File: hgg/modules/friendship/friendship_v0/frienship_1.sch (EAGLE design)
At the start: 35 parts, among them IC5 741G66DBV, IC6 741G66DBV, IC7 741G66DBV, IC8 741G66DBV

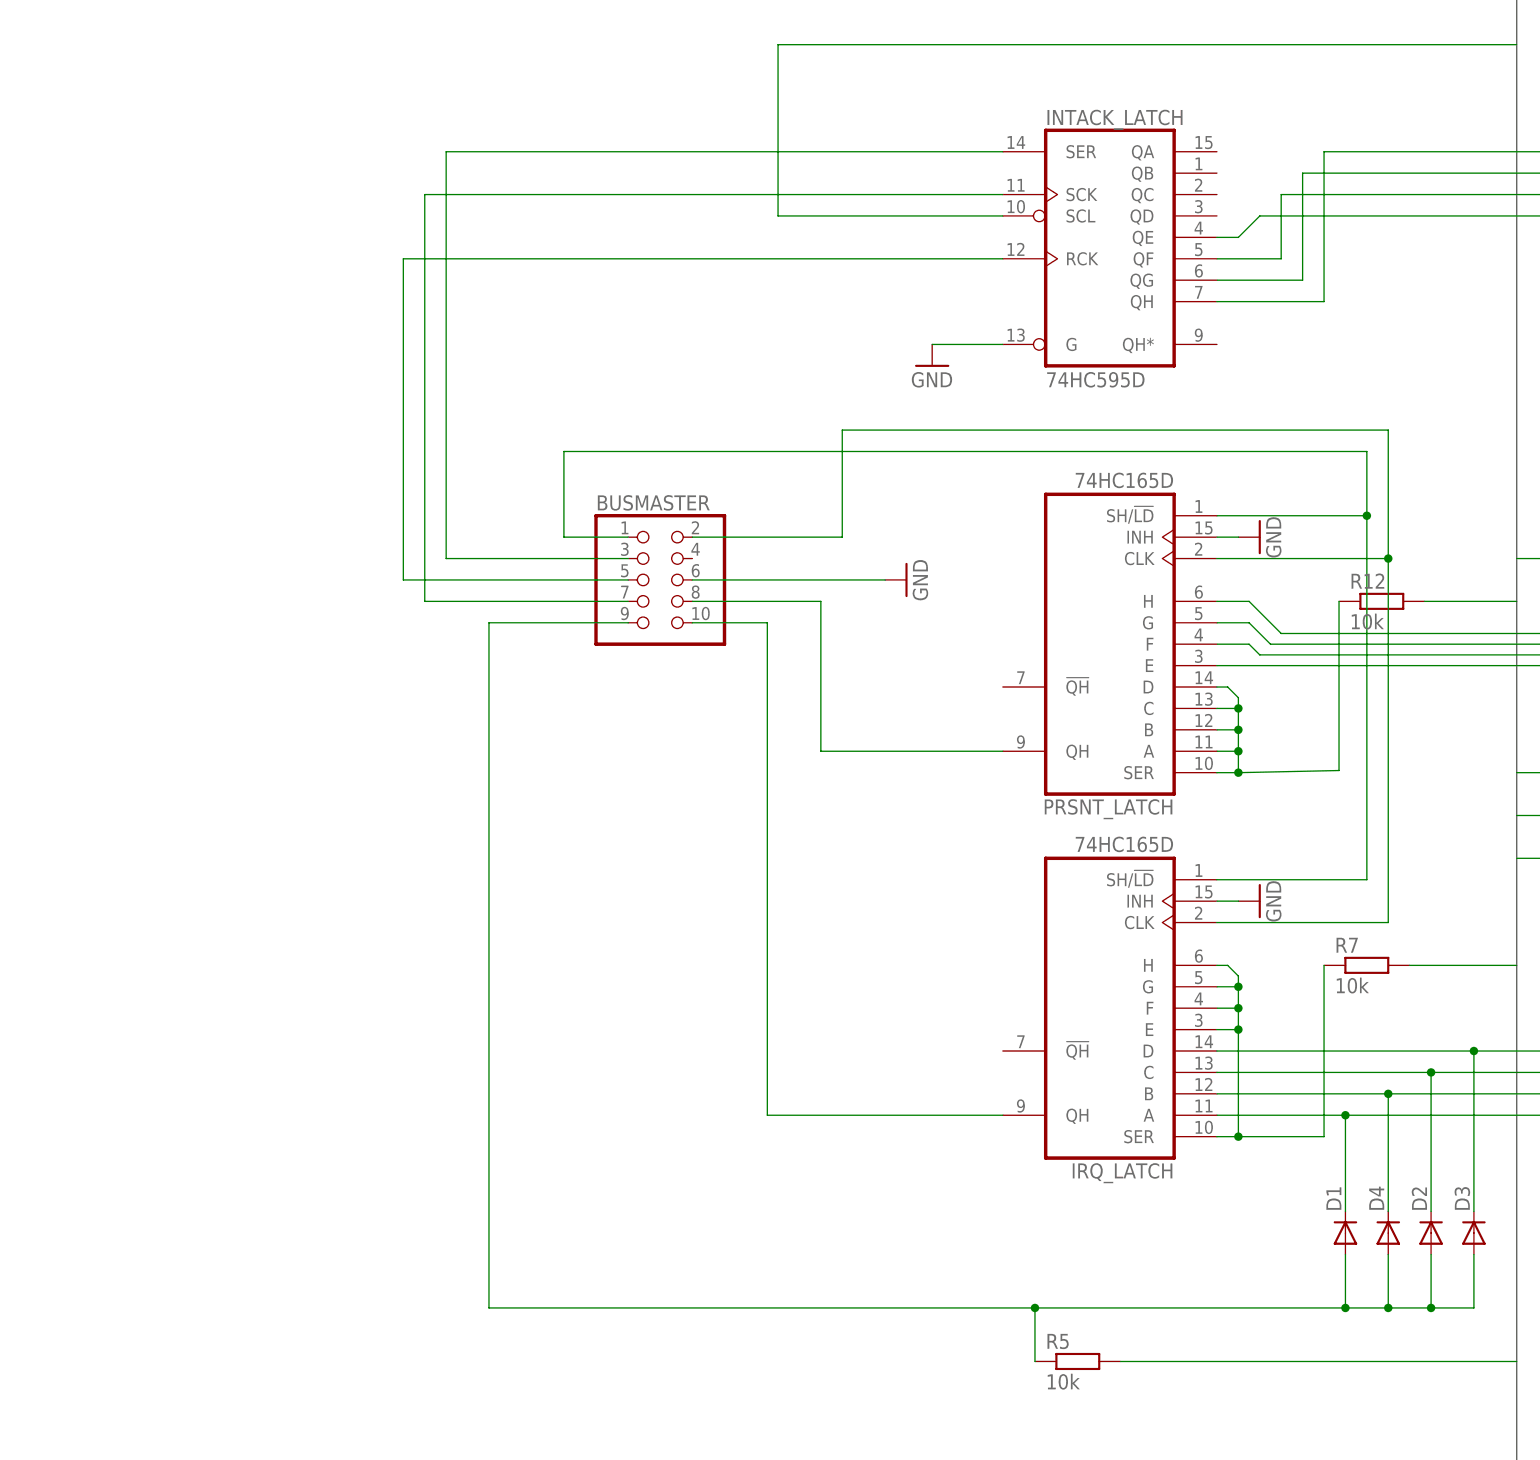
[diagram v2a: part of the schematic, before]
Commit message: using new busmaster plug, more ground vias
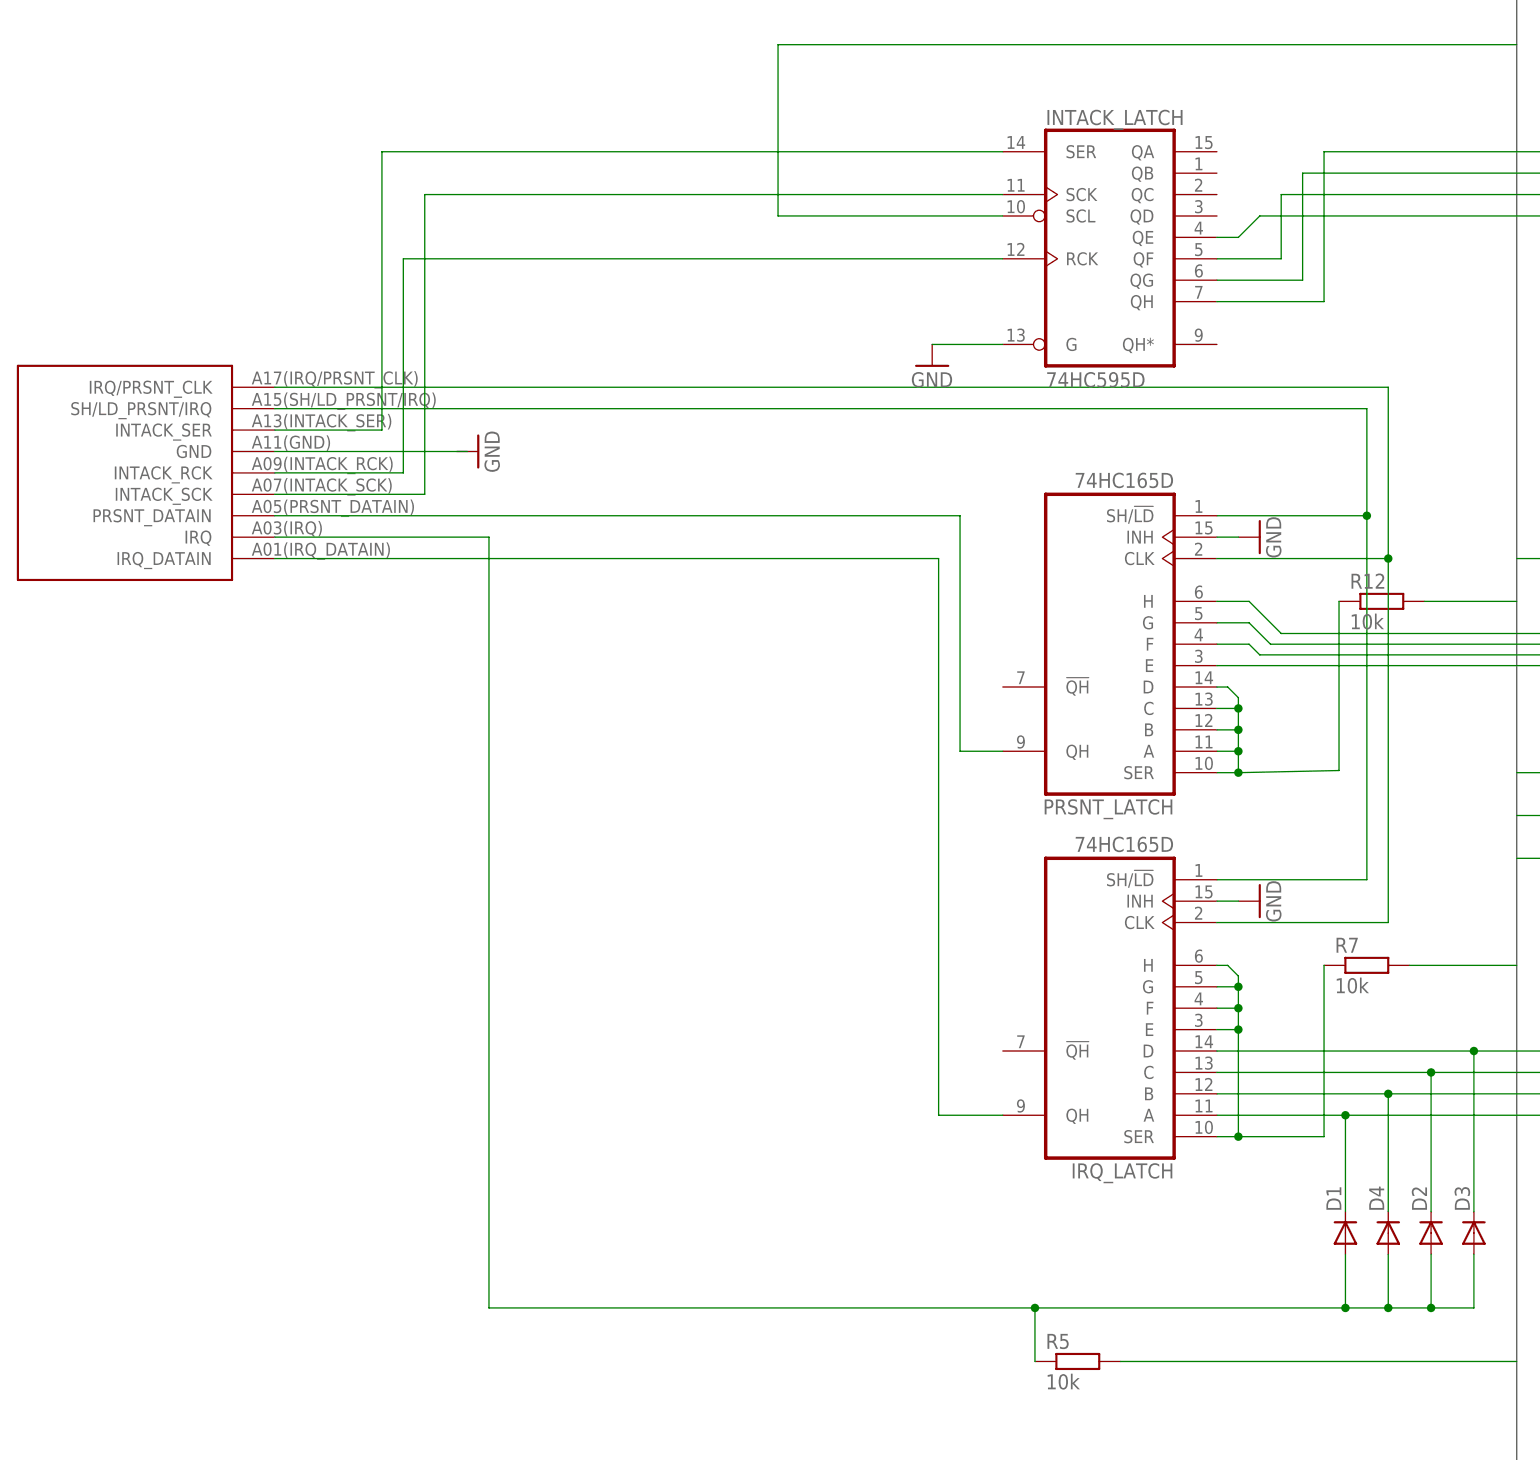
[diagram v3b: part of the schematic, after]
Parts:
- removed BUSMASTER: (no value), pinhead:PINHD-2X5
- added U$1: BUSMASTER_PLUG, hgg:BUSMASTER_PLUG
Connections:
- new net N$12: U$1.GND
- net GND: no longer BUSMASTER.6
- net N$1: now also U$1.INTACK_SER; no longer BUSMASTER.3
- net N$11: now also U$1.IRQ; no longer BUSMASTER.9
- net N$13: now also U$1.PRSNT_DATAIN; no longer BUSMASTER.8
- net N$17: now also U$1.IRQ_DATAIN; no longer BUSMASTER.10
- net N$3: now also U$1.SH/LD_PRSNT/IRQ; no longer BUSMASTER.1
- net N$4: now also U$1.INTACK_SCK; no longer BUSMASTER.7
- net N$9: now also U$1.INTACK_RCK; no longer BUSMASTER.5
- net SHIFT: now also U$1.IRQ/PRSNT_CLK; no longer BUSMASTER.2
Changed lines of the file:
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@@
 <setting verticaltext="up"/>
 </settings>
-<grid distance="0.05" unitdist="inch" unit="inch" style="lines" multiple="1" display="no" altdistance="0.01" altunitdist="inch" altunit="inch"/>
+<grid distance="0.1" unitdist="inch" unit="inch" style="lines" multiple="1" display="no" altdistance="0.01" altunitdist="inch" altunit="inch"/>
 <layers>
 <layer number="1" name="Top" color="4" fill="1" visible="no" active="no"/>
@@
 <part name="IRQ_LATCH" library="74xx-eu" deviceset="74*165" device="D" technology="HC"/>
 <part name="PRSNT_LATCH" library="74xx-eu" deviceset="74*165" device="D" technology="HC"/>
-<part name="BUSMASTER" library="pinhead" deviceset="PINHD-2X5" device=""/>
 <part name="R7" library="rcl" deviceset="R-EU_" device="R0603" value="10k"/>
 <part name="R12" library="rcl" deviceset="R-EU_" device="R0603" value="10k"/>
@@
 <part name="R16" library="rcl" deviceset="R-EU_" device="R0603" value="10k"/>
 <part name="R17" library="rcl" deviceset="R-EU_" device="R0603" value="10k"/>
+<part name="U$1" library="hgg" deviceset="BUSMASTER_PLUG" device=""/>
 </parts>
 <sheets>
@@
 <instance part="IRQ_LATCH" gate="A" x="-157.48" y="-86.36" rot="R180"/>
 <instance part="PRSNT_LATCH" gate="A" x="-157.48" y="-43.18" rot="R180"/>
-<instance part="BUSMASTER" gate="A" x="-212.09" y="-35.56"/>
 <instance part="R7" gate="G$1" x="-127" y="-81.28"/>
 <instance part="R12" gate="G$1" x="-125.222" y="-38.1"/>
@@
 <instance part="D3" gate="G$1" x="-114.3" y="-113.03" rot="R90"/>
 <instance part="D4" gate="G$1" x="-124.46" y="-113.03" rot="R90"/>
-<instance part="GND18" gate="1" x="-181.61" y="-35.56" rot="R90"/>
+<instance part="GND18" gate="1" x="-232.41" y="-20.32" rot="R90"/>
 <instance part="R5" gate="G$1" x="-161.29" y="-128.27"/>
 <instance part="SJ1" gate="1" x="-63.5" y="-302.26"/>
@@
 <instance part="R16" gate="G$1" x="-228.6" y="182.88" rot="R90"/>
 <instance part="R17" gate="G$1" x="-220.98" y="182.88" rot="R90"/>
+<instance part="U$1" gate="G$1" x="-261.62" y="-12.7" rot="R180"/>
 </instances>
 <busses>
@@
 <wire x1="15.24" y1="-185.42" x2="76.2" y2="-185.42" width="0.1524" layer="91"/>
 <junction x="15.24" y="-185.42"/>
-</segment>
-<segment>
-<pinref part="BUSMASTER" gate="A" pin="6"/>
-<wire x1="-207.01" y1="-35.56" x2="-184.15" y2="-35.56" width="0.1524" layer="91"/>
-<pinref part="GND18" gate="1" pin="GND"/>
 </segment>
 <segment>
@@
 <wire x1="-144.78" y1="-33.02" x2="-124.46" y2="-33.02" width="0.1524" layer="91"/>
 <wire x1="-124.46" y1="-76.2" x2="-124.46" y2="-33.02" width="0.1524" layer="91"/>
-<pinref part="BUSMASTER" gate="A" pin="2"/>
-<wire x1="-207.01" y1="-30.48" x2="-189.23" y2="-30.48" width="0.1524" layer="91"/>
-<wire x1="-189.23" y1="-30.48" x2="-189.23" y2="-17.78" width="0.1524" layer="91"/>
-<wire x1="-189.23" y1="-17.78" x2="-124.46" y2="-17.78" width="0.1524" layer="91"/>
-<wire x1="-124.46" y1="-17.78" x2="-124.46" y2="-33.02" width="0.1524" layer="91"/>
+<wire x1="-124.46" y1="-12.7" x2="-124.46" y2="-33.02" width="0.1524" layer="91"/>
 <junction x="-124.46" y="-33.02"/>
 <pinref part="IRQ_LATCH" gate="A" pin="CLK"/>
 <wire x1="-144.78" y1="-76.2" x2="-124.46" y2="-76.2" width="0.1524" layer="91"/>
+<pinref part="U$1" gate="G$1" pin="IRQ/PRSNT_CLK"/>
+<wire x1="-256.54" y1="-12.7" x2="-124.46" y2="-12.7" width="0.1524" layer="91"/>
 </segment>
 </net>
@@
 <segment>
 <pinref part="PRSNT_LATCH" gate="A" pin="QH"/>
-<wire x1="-170.18" y1="-55.88" x2="-191.77" y2="-55.88" width="0.1524" layer="91"/>
-<pinref part="BUSMASTER" gate="A" pin="8"/>
-<wire x1="-207.01" y1="-38.1" x2="-191.77" y2="-38.1" width="0.1524" layer="91"/>
-<wire x1="-191.77" y1="-38.1" x2="-191.77" y2="-55.88" width="0.1524" layer="91"/>
+<wire x1="-170.18" y1="-55.88" x2="-175.26" y2="-55.88" width="0.1524" layer="91"/>
+<pinref part="U$1" gate="G$1" pin="PRSNT_DATAIN"/>
+<wire x1="-256.54" y1="-27.94" x2="-175.26" y2="-27.94" width="0.1524" layer="91"/>
+<wire x1="-175.26" y1="-27.94" x2="-175.26" y2="-55.88" width="0.1524" layer="91"/>
 </segment>
 </net>
@@
 <segment>
 <pinref part="IRQ_LATCH" gate="A" pin="QH"/>
-<wire x1="-170.18" y1="-99.06" x2="-198.12" y2="-99.06" width="0.1524" layer="91"/>
-<pinref part="BUSMASTER" gate="A" pin="10"/>
-<wire x1="-207.01" y1="-40.64" x2="-198.12" y2="-40.64" width="0.1524" layer="91"/>
-<wire x1="-198.12" y1="-40.64" x2="-198.12" y2="-99.06" width="0.1524" layer="91"/>
+<wire x1="-170.18" y1="-99.06" x2="-177.8" y2="-99.06" width="0.1524" layer="91"/>
+<pinref part="U$1" gate="G$1" pin="IRQ_DATAIN"/>
+<wire x1="-256.54" y1="-33.02" x2="-177.8" y2="-33.02" width="0.1524" layer="91"/>
+<wire x1="-177.8" y1="-33.02" x2="-177.8" y2="-99.06" width="0.1524" layer="91"/>
 </segment>
 </net>
 <net name="N$3" class="0">
 <segment>
-<wire x1="-222.25" y1="-20.32" x2="-127" y2="-20.32" width="0.1524" layer="91"/>
-<wire x1="-127" y1="-20.32" x2="-127" y2="-27.94" width="0.1524" layer="91"/>
+<wire x1="-127" y1="-15.24" x2="-127" y2="-27.94" width="0.1524" layer="91"/>
 <pinref part="PRSNT_LATCH" gate="A" pin="SH/!LD"/>
 <wire x1="-144.78" y1="-27.94" x2="-127" y2="-27.94" width="0.1524" layer="91"/>
@@
 <pinref part="IRQ_LATCH" gate="A" pin="SH/!LD"/>
 <wire x1="-127" y1="-71.12" x2="-144.78" y2="-71.12" width="0.1524" layer="91"/>
-<pinref part="BUSMASTER" gate="A" pin="1"/>
-<wire x1="-222.25" y1="-20.32" x2="-222.25" y2="-30.48" width="0.1524" layer="91"/>
-<wire x1="-222.25" y1="-30.48" x2="-214.63" y2="-30.48" width="0.1524" layer="91"/>
+<pinref part="U$1" gate="G$1" pin="SH/LD_PRSNT/IRQ"/>
+<wire x1="-256.54" y1="-15.24" x2="-127" y2="-15.24" width="0.1524" layer="91"/>
 </segment>
 </net>
@@
 <segment>
 <pinref part="INTACK_LATCH" gate="A" pin="SER"/>
-<wire x1="-170.18" y1="15.24" x2="-236.22" y2="15.24" width="0.1524" layer="91"/>
-<wire x1="-236.22" y1="15.24" x2="-236.22" y2="-33.02" width="0.1524" layer="91"/>
-<pinref part="BUSMASTER" gate="A" pin="3"/>
-<wire x1="-236.22" y1="-33.02" x2="-214.63" y2="-33.02" width="0.1524" layer="91"/>
+<wire x1="-170.18" y1="15.24" x2="-243.84" y2="15.24" width="0.1524" layer="91"/>
+<pinref part="U$1" gate="G$1" pin="INTACK_SER"/>
+<wire x1="-256.54" y1="-17.78" x2="-243.84" y2="-17.78" width="0.1524" layer="91"/>
+<wire x1="-243.84" y1="-17.78" x2="-243.84" y2="15.24" width="0.1524" layer="91"/>
 </segment>
 </net>
@@
 <pinref part="INTACK_LATCH" gate="A" pin="SCK"/>
 <wire x1="-170.18" y1="10.16" x2="-238.76" y2="10.16" width="0.1524" layer="91"/>
-<wire x1="-238.76" y1="10.16" x2="-238.76" y2="-38.1" width="0.1524" layer="91"/>
-<pinref part="BUSMASTER" gate="A" pin="7"/>
-<wire x1="-238.76" y1="-38.1" x2="-214.63" y2="-38.1" width="0.1524" layer="91"/>
+<wire x1="-238.76" y1="10.16" x2="-238.76" y2="-25.4" width="0.1524" layer="91"/>
+<pinref part="U$1" gate="G$1" pin="INTACK_SCK"/>
+<wire x1="-256.54" y1="-25.4" x2="-238.76" y2="-25.4" width="0.1524" layer="91"/>
 </segment>
 </net>
@@
 <pinref part="INTACK_LATCH" gate="A" pin="RCK"/>
 <wire x1="-170.18" y1="2.54" x2="-241.3" y2="2.54" width="0.1524" layer="91"/>
-<wire x1="-241.3" y1="2.54" x2="-241.3" y2="-35.56" width="0.1524" layer="91"/>
-<pinref part="BUSMASTER" gate="A" pin="5"/>
-<wire x1="-241.3" y1="-35.56" x2="-214.63" y2="-35.56" width="0.1524" layer="91"/>
+<wire x1="-241.3" y1="2.54" x2="-241.3" y2="-22.86" width="0.1524" layer="91"/>
+<pinref part="U$1" gate="G$1" pin="INTACK_RCK"/>
+<wire x1="-256.54" y1="-22.86" x2="-241.3" y2="-22.86" width="0.1524" layer="91"/>
 </segment>
 </net>
@@
 <wire x1="-129.54" y1="-121.92" x2="-166.37" y2="-121.92" width="0.1524" layer="91"/>
 <wire x1="-166.37" y1="-121.92" x2="-231.14" y2="-121.92" width="0.1524" layer="91"/>
-<wire x1="-231.14" y1="-121.92" x2="-231.14" y2="-40.64" width="0.1524" layer="91"/>
+<wire x1="-231.14" y1="-121.92" x2="-231.14" y2="-30.48" width="0.1524" layer="91"/>
 <junction x="-129.54" y="-121.92"/>
-<pinref part="BUSMASTER" gate="A" pin="9"/>
-<wire x1="-231.14" y1="-40.64" x2="-214.63" y2="-40.64" width="0.1524" layer="91"/>
 <pinref part="R5" gate="G$1" pin="1"/>
 <wire x1="-166.37" y1="-128.27" x2="-166.37" y2="-121.92" width="0.1524" layer="91"/>
 <junction x="-166.37" y="-121.92"/>
+<pinref part="U$1" gate="G$1" pin="IRQ"/>
+<wire x1="-256.54" y1="-30.48" x2="-231.14" y2="-30.48" width="0.1524" layer="91"/>
 </segment>
 </net>
@@
 </segment>
 </net>
+<net name="N$12" class="0">
+<segment>
+<pinref part="U$1" gate="G$1" pin="GND"/>
+<wire x1="-233.68" y1="-20.32" x2="-256.54" y2="-20.32" width="0.1524" layer="91"/>
+</segment>
+</net>
